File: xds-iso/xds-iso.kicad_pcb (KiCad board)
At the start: 2 copper layers, 82 x 33 mm, 109 parts, among them J1 USB4085, J2 TGT_JTAG, J3 IF_JTAG, J4 Conn_01x02_Male, SW2 EVQPUD, U1 MCP1703A-3002_SOT223, U2 MSP432E401Y, U3 ISOW7741, U4 ISOW7741, U5 TPD4E004DRYR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

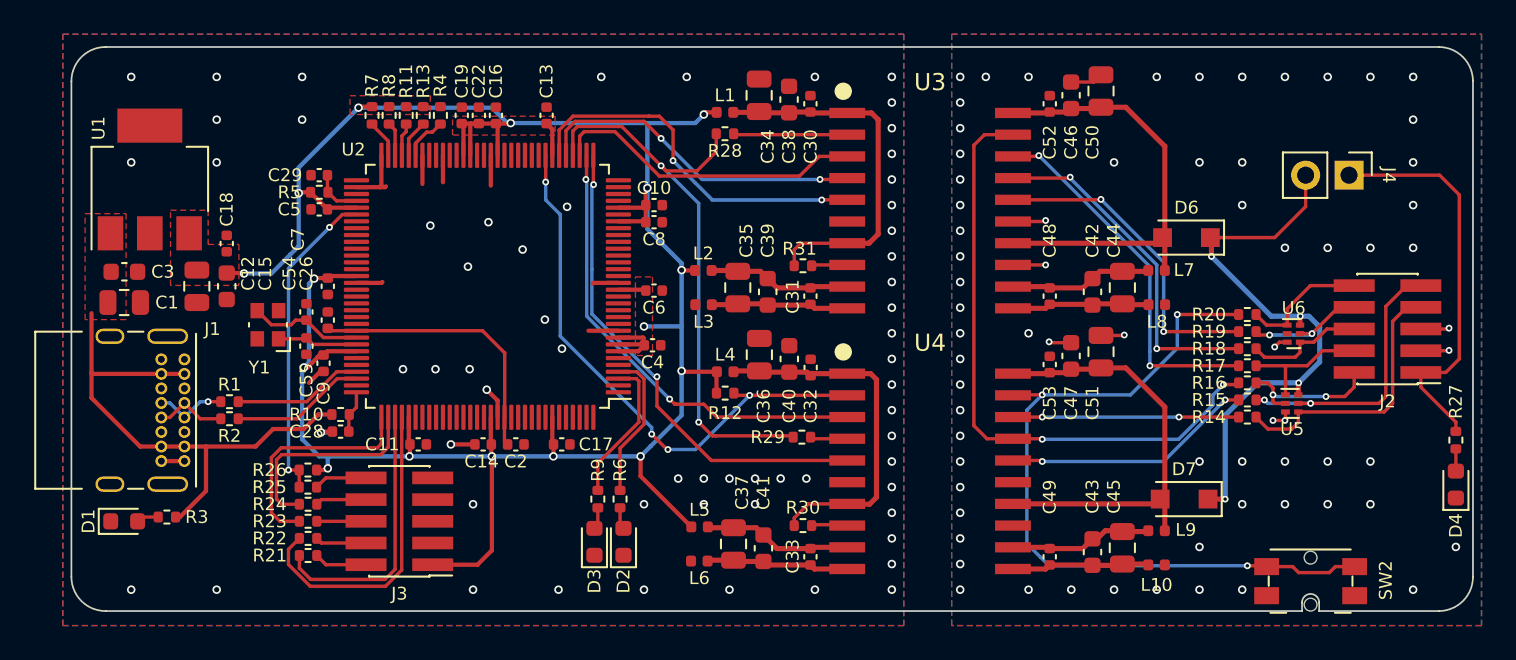
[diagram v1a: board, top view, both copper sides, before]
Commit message: R02 updates supporting cJTAG and SWD
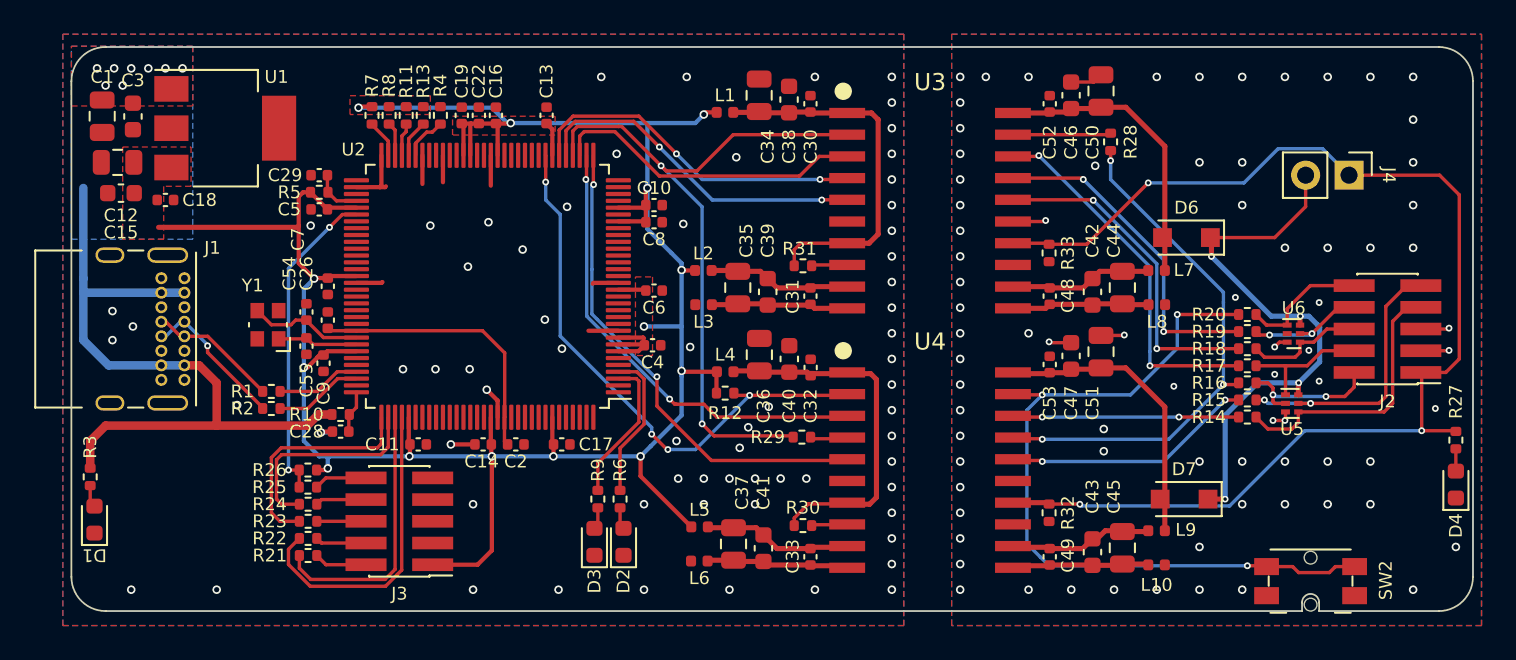
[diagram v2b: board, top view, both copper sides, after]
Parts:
- added R32: 10k, Resistor_SMD:R_0402_1005Metric, F.Cu at (158.7, 103.0)
- added R33: 10k, Resistor_SMD:R_0402_1005Metric, F.Cu at (158.7, 87.8)
- R28: value 100R -> 1K
- R29: value 100R-DNP -> 100R
- U4: value ISOW7741 -> ISOW7742
- moved R28 22.6 mm to (162.3, 81.3), turned to -90 degrees
- moved C1 11.0 mm to (103.3, 79.8), turned to 90 degrees
- moved C3 9.10 mm to (105.1, 79.8), turned to 90 degrees
- moved C12 8.61 mm to (104.2, 82.5), turned to 0 degrees
- moved C15 8.25 mm to (104.4, 84.3), turned to 0 degrees
- moved U1 5.34 mm to (110.5, 80.5), turned to 0 degrees
- moved R3 5.07 mm to (102.6, 100.9), turned to 90 degrees
- moved J1 4.75 mm to (108.1, 89.3)
- moved C18 4.40 mm to (107.0, 84.7), turned to 180 degrees
- moved R1 2.52 mm to (113.2, 95.9)
- moved R2 2.52 mm to (113.2, 96.9)
- moved D1 1.74 mm to (102.8, 103.4), turned to 90 degrees
- moved U4 0.07 mm to (151.7, 100.5)
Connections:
- R28 pad 1: /XDS_TMS -> Net-(R28-Pad1)
- R28 pad 2: Net-(R28-Pad2) -> /ISO_TMS
- U3 pad 14: Net-(C46-Pad1) -> /V_{TGT}
- U3 pad 16: /ISO_TDI -> /ISO_TDO
- U3 pad 17: /ISO_TDO -> /ISO_TDI
- U3 pad 19: /ISO_TMS -> Net-(R28-Pad1)
- U3 pad 2: Net-(R28-Pad2) -> /XDS_TMS
- U3 pad 4: /XDS_TDO -> /XDS_TDI
- U3 pad 5: /XDS_TDI -> /XDS_TDO
- U4 pad 14: Net-(C47-Pad1) -> /V_{TGT}
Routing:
- net /V_{TGT}: track 23.4 -> 72.9 mm, vias 0 -> 3
- net +5V: track 31.4 -> 42.5 mm, vias 0 -> 8
- net Net-(C46-Pad1): track 26.2 -> 17.3 mm
- net Net-(C47-Pad1): track 26.1 -> 17.3 mm
- net /XDS_TMS: track 34.3 -> 41.3 mm
- net Net-(R28-Pad2): track 6.66 -> 0.00 mm
- net Net-(R28-Pad1): track 0.00 -> 5.75 mm
- net /ISO_TMS: track 36.5 -> 31.0 mm, vias 2 -> 3
- net Net-(J1-PadA6): track 4.21 -> 8.67 mm, vias 0 -> 1
- net Net-(J1-PadA7): track 4.21 -> 7.62 mm, vias 1 -> 0
- net /USB_DM: track 7.64 -> 4.94 mm
- net /USB_DP: track 7.89 -> 5.19 mm
- net GND: track 20.7 -> 18.2 mm, vias 61 -> 67
- net GND1: track 13.8 -> 11.9 mm, vias 69 -> 77
- net /XDS_TDI: track 21.8 -> 20.2 mm
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- added copper zone on B.Cu, net +5V
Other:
- board text added: "r0.2"
- board text removed: "r0.1"

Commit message: Changed TMS series resistor to 1k
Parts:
- R29: value 100R -> 1k
- U1: value MCP1703A-3002_SOT223 -> AP7361EA-33E-13
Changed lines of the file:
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@@
       (effects (font (size 0.75 0.75) (thickness 0.15)))
     )
-    (fp_text value "MCP1703A-3002_SOT223" (at 0 4.5) (layer "F.Fab")
+    (fp_text value "AP7361EA-33E-13" (at 0 4.5) (layer "F.Fab")
       (effects (font (size 1 1) (thickness 0.15)))
     )
@@
       (effects (font (size 0.75 0.75) (thickness 0.15)))
     )
-    (fp_text value "100R" (at 0 1.17) (layer "F.Fab")
-      (effects (font (size 1 1) (thickness 0.15)))
-    )
+    (fp_text value "1k" (at 0 1.17) (layer "F.Fab")
+      (effects (font (size 1 1) (thickness 0.15)))
+    )

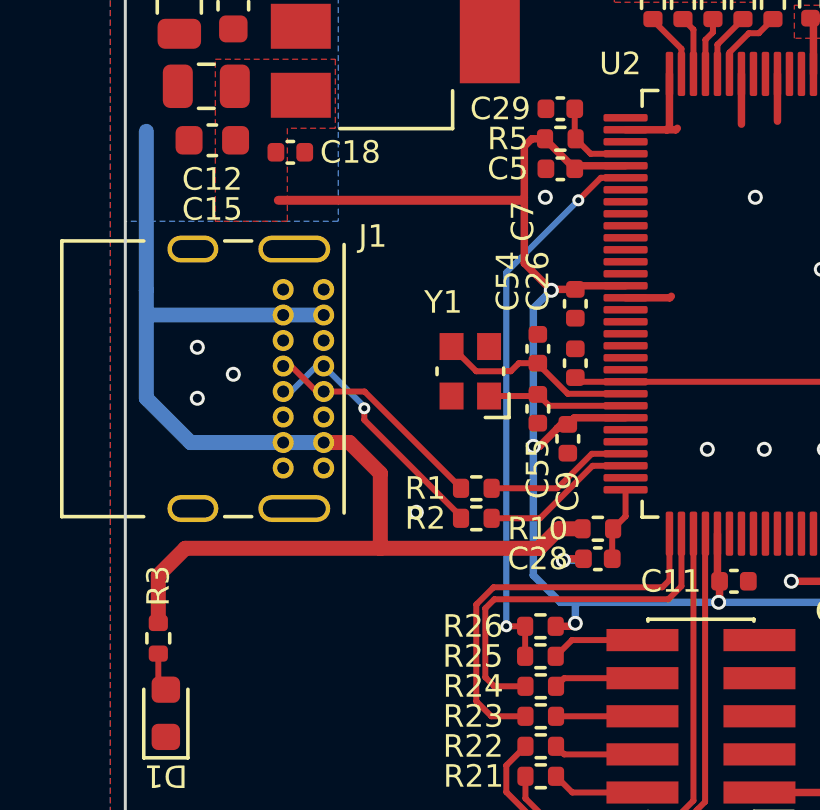
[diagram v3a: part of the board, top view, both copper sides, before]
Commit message: Added 5.1k pulldowns to the CC1 and CC2 pins to comply with USB Type C spec
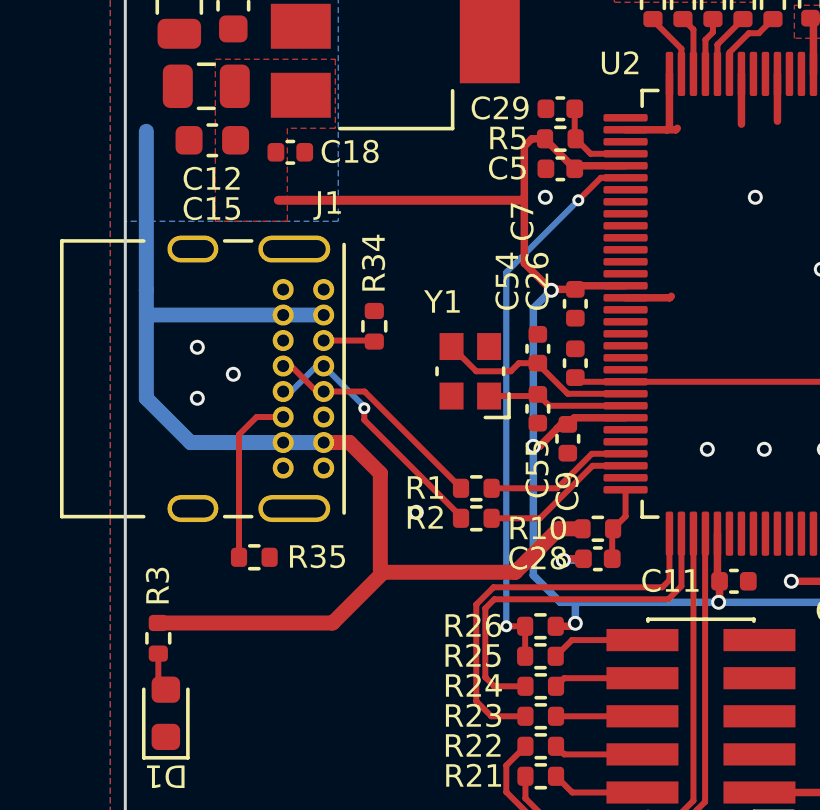
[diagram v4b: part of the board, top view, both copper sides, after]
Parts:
- added R34: 5.1k, Resistor_SMD:R_0402_1005Metric, F.Cu at (109.8, 90.5)
- added R35: 5.1k, Resistor_SMD:R_0402_1005Metric, F.Cu at (105.8, 98.2)
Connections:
- J1 pad A5: unconnected-(J1-PadA5) -> /CC1
- J1 pad B5: unconnected-(J1-PadB5) -> /CC2
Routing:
- net /CC2: track 0.00 -> 5.80 mm
- net /CC1: track 0.00 -> 1.70 mm
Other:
- board text added: "r0.2b"
- board text removed: "r0.2"
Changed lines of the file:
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@@
     )
     (pad_to_mask_clearance 0)
+    (grid_origin 110 87.5)
     (pcbplotparams
       (layerselection 0x00010fc_ffffffff)
@@
   (net 23 "Net-(D4-Pad2)")
   (net 24 "/V_{ISOOUT}")
-  (net 25 "unconnected-(J1-PadA5)")
+  (net 25 "/CC1")
   (net 26 "Net-(J1-PadA6)")
   (net 27 "Net-(J1-PadA7)")
   (net 28 "unconnected-(J1-PadA8)")
-  (net 29 "unconnected-(J1-PadB5)")
+  (net 29 "/CC2")
   (net 30 "unconnected-(J1-PadB8)")
   (net 31 "/V_{TGT}")
@@
     (property "Sheetname" "")
     (attr through_hole)
-    (fp_text reference "J1" (at -1.775 -1.6375 unlocked) (layer "F.SilkS")
+    (fp_text reference "J1" (at -2.875 -0.1875 unlocked) (layer "F.SilkS")
       (effects (font (size 0.75 0.75) (thickness 0.15)))
     )
@@
       (net 2 "+5V") (pinfunction "VBUS") (pintype "passive"))
     (pad "A5" thru_hole circle (at 1.7 0 270) (size 0.7 0.7) (drill 0.4) (layers *.Cu *.Mask)
-      (net 25 "unconnected-(J1-PadA5)") (pinfunction "CC1") (pintype "bidirectional+no_connect"))
+      (net 25 "/CC1") (pinfunction "CC1") (pintype "bidirectional"))
     (pad "A6" thru_hole circle (at 2.55 0 270) (size 0.7 0.7) (drill 0.4) (layers *.Cu *.Mask)
       (net 26 "Net-(J1-PadA6)") (pinfunction "D+") (pintype "bidirectional"))
@@
       (net 2 "+5V") (pinfunction "VBUS") (pintype "passive"))
     (pad "B5" thru_hole circle (at 4.25 1.35 270) (size 0.7 0.7) (drill 0.4) (layers *.Cu *.Mask)
-      (net 29 "unconnected-(J1-PadB5)") (pinfunction "CC2") (pintype "bidirectional+no_connect"))
+      (net 29 "/CC2") (pinfunction "CC2") (pintype "bidirectional"))
     (pad "B6" thru_hole circle (at 3.4 1.35 270) (size 0.7 0.7) (drill 0.4) (layers *.Cu *.Mask)
       (net 26 "Net-(J1-PadA6)") (pinfunction "D+") (pintype "bidirectional"))
@@
   )
   (footprint "Resistor_SMD:R_0402_1005Metric" (layer "F.Cu")
+    (at 109.8 90.5 -90)
+    (descr "Resistor SMD 0402 (1005 Metric), square (rectangular) end terminal, IPC_7351 nominal, (Body size source: IPC-SM-782 page 72, https://www.pcb-3d.com/wordpress/wp-content/uploads/ipc-sm-782a_amendment_1_and_2.pdf), generated with kicad-footprint-generator")
+    (tags "resistor")
+    (property "Sheetfile" "xds-iso.kicad_sch")
+    (property "Sheetname" "")
+    (attr smd)
+    (fp_text reference "R34" (at -2.1 0 90) (layer "F.SilkS")
+      (effects (font (size 0.75 0.75) (thickness 0.15)))
+    )
+    (fp_text value "5.1k" (at 0 1.17 90) (layer "F.Fab")
+      (effects (font (size 1 1) (thickness 0.15)))
+    )
+    (fp_text user "${REFERENCE}" (at 0 0 90) (layer "F.Fab")
+      (effects (font (size 0.26 0.26) (thickness 0.04)))
+    )
+    (fp_line (start -0.153641 0.38) (end 0.153641 0.38) (layer "F.SilkS") (width 0.12))
+    (fp_line (start -0.153641 -0.38) (end 0.153641 -0.38) (layer "F.SilkS") (width 0.12))
+    (fp_line (start -0.93 -0.47) (end 0.93 -0.47) (layer "F.CrtYd") (width 0.05))
+    (fp_line (start -0.93 0.47) (end -0.93 -0.47) (layer "F.CrtYd") (width 0.05))
+    (fp_line (start 0.93 -0.47) (end 0.93 0.47) (layer "F.CrtYd") (width 0.05))
+    (fp_line (start 0.93 0.47) (end -0.93 0.47) (layer "F.CrtYd") (width 0.05))
+    (fp_line (start -0.525 0.27) (end -0.525 -0.27) (layer "F.Fab") (width 0.1))
+    (fp_line (start 0.525 -0.27) (end 0.525 0.27) (layer "F.Fab") (width 0.1))
+    (fp_line (start 0.525 0.27) (end -0.525 0.27) (layer "F.Fab") (width 0.1))
+    (fp_line (start -0.525 -0.27) (end 0.525 -0.27) (layer "F.Fab") (width 0.1))
+    (pad "1" smd roundrect (at -0.51 0 270) (size 0.54 0.64) (layers "F.Cu" "F.Paste" "F.Mask") (roundrect_rratio 0.25)
+      (net 1 "GND") (pintype "passive"))
+    (pad "2" smd roundrect (at 0.51 0 270) (size 0.54 0.64) (layers "F.Cu" "F.Paste" "F.Mask") (roundrect_rratio 0.25)
+      (net 25 "/CC1") (pintype "passive"))
+    (model "${KICAD6_3DMODEL_DIR}/Resistor_SMD.3dshapes/R_0402_1005Metric.wrl"
+      (offset (xyz 0 0 0))
+      (scale (xyz 1 1 1))
+      (rotate (xyz 0 0 0))
+    )
+  )
+  (footprint "Resistor_SMD:R_0402_1005Metric" (layer "F.Cu")
     (at 170.3 97.4)
     (descr "Resistor SMD 0402 (1005 Metric), square (rectangular) end terminal, IPC_7351 nominal, (Body size source: IPC-SM-782 page 72, https://www.pcb-3d.com/wordpress/wp-content/uploads/ipc-sm-782a_amendment_1_and_2.pdf), generated with kicad-footprint-generator")
@@
   )
   (footprint "Resistor_SMD:R_0402_1005Metric" (layer "F.Cu")
+    (at 105.8 98.2 180)
+    (descr "Resistor SMD 0402 (1005 Metric), square (rectangular) end terminal, IPC_7351 nominal, (Body size source: IPC-SM-782 page 72, https://www.pcb-3d.com/wordpress/wp-content/uploads/ipc-sm-782a_amendment_1_and_2.pdf), generated with kicad-footprint-generator")
+    (tags "resistor")
+    (property "Sheetfile" "xds-iso.kicad_sch")
+    (property "Sheetname" "")
+    (attr smd)
+    (fp_text reference "R35" (at -2.1 0) (layer "F.SilkS")
+      (effects (font (size 0.75 0.75) (thickness 0.15)))
+    )
+    (fp_text value "5.1k" (at 0 1.17) (layer "F.Fab")
+      (effects (font (size 1 1) (thickness 0.15)))
+    )
+    (fp_text user "${REFERENCE}" (at 0 0) (layer "F.Fab")
+      (effects (font (size 0.26 0.26) (thickness 0.04)))
+    )
+    (fp_line (start -0.153641 -0.38) (end 0.153641 -0.38) (layer "F.SilkS") (width 0.12))
+    (fp_line (start -0.153641 0.38) (end 0.153641 0.38) (layer "F.SilkS") (width 0.12))
+    (fp_line (start -0.93 0.47) (end -0.93 -0.47) (layer "F.CrtYd") (width 0.05))
+    (fp_line (start 0.93 0.47) (end -0.93 0.47) (layer "F.CrtYd") (width 0.05))
+    (fp_line (start -0.93 -0.47) (end 0.93 -0.47) (layer "F.CrtYd") (width 0.05))
+    (fp_line (start 0.93 -0.47) (end 0.93 0.47) (layer "F.CrtYd") (width 0.05))
+    (fp_line (start 0.525 0.27) (end -0.525 0.27) (layer "F.Fab") (width 0.1))
+    (fp_line (start 0.525 -0.27) (end 0.525 0.27) (layer "F.Fab") (width 0.1))
+    (fp_line (start -0.525 0.27) (end -0.525 -0.27) (layer "F.Fab") (width 0.1))
+    (fp_line (start -0.525 -0.27) (end 0.525 -0.27) (layer "F.Fab") (width 0.1))
+    (pad "1" smd roundrect (at -0.51 0 180) (size 0.54 0.64) (layers "F.Cu" "F.Paste" "F.Mask") (roundrect_rratio 0.25)
+      (net 1 "GND") (pintype "passive"))
+    (pad "2" smd roundrect (at 0.51 0 180) (size 0.54 0.64) (layers "F.Cu" "F.Paste" "F.Mask") (roundrect_rratio 0.25)
+      (net 29 "/CC2") (pintype "passive"))
+    (model "${KICAD6_3DMODEL_DIR}/Resistor_SMD.3dshapes/R_0402_1005Metric.wrl"
+      (offset (xyz 0 0 0))
+      (scale (xyz 1 1 1))
+      (rotate (xyz 0 0 0))
+    )
+  )
+  (footprint "Resistor_SMD:R_0402_1005Metric" (layer "F.Cu")
     (at 170.3 91.4 180)
     (descr "Resistor SMD 0402 (1005 Metric), square (rectangular) end terminal, IPC_7351 nominal, (Body size source: IPC-SM-782 page 72, https://www.pcb-3d.com/wordpress/wp-content/uploads/ipc-sm-782a_amendment_1_and_2.pdf), generated with kicad-footprint-generator")
@@
     (effects (font (size 1 1) (thickness 0.15)) (justify mirror))
   )
-  (gr_text "r0.2" (at 154.6 92.25 90) (layer "B.Mask")
+  (gr_text "r0.2b" (at 154.6 92.25 90) (layer "B.Mask")
     (effects (font (size 1 1) (thickness 0.25)) (justify mirror))
   )
@@
   (segment (start 116.1 98.3) (end 116.7 98.3) (width 0.25) (layer "B.Cu") (net 1))
   (segment (start 116.7 98.3) (end 116.8 98.2) (width 0.25) (layer "B.Cu") (net 1))
-  (segment (start 103.5 97.9) (end 102.6 98.8) (width 0.5) (layer "F.Cu") (net 2))
-  (segment (start 110 97.9) (end 103.5 97.9) (width 0.5) (layer "F.Cu") (net 2))
-  (segment (start 110 95.4) (end 110 97.9) (width 0.5) (layer "F.Cu") (net 2))
-  (segment (start 110 97.9) (end 115.3 97.9) (width 0.5) (layer "F.Cu") (net 2))
-  (segment (start 115.3 97.9) (end 115.95 97.25) (width 0.5) (layer "F.Cu") (net 2))
+  (segment (start 110 98.6) (end 110.1 98.7) (width 0.5) (layer "F.Cu") (net 2))
+  (segment (start 116.74 97.25) (end 115.95 97.25) (width 0.5) (layer "F.Cu") (net 2))
+  (segment (start 110.1 98.7) (end 108.41 100.39) (width 0.5) (layer "F.Cu") (net 2))
   (segment (start 108.975 94.375) (end 110 95.4) (width 0.5) (layer "F.Cu") (net 2))
-  (segment (start 102.6 98.8) (end 102.6 100.39) (width 0.5) (layer "F.Cu") (net 2))
-  (segment (start 115.95 97.25) (end 116.74 97.25) (width 0.5) (layer "F.Cu") (net 2))
+  (segment (start 110 95.4) (end 110 98.6) (width 0.5) (layer "F.Cu") (net 2))
+  (segment (start 115.95 97.25) (end 114.5 98.7) (width 0.5) (layer "F.Cu") (net 2))
+  (segment (start 114.5 98.7) (end 110.1 98.7) (width 0.5) (layer "F.Cu") (net 2))
+  (segment (start 108.41 100.39) (end 102.6 100.39) (width 0.5) (layer "F.Cu") (net 2))
   (segment (start 108.1125 94.375) (end 108.975 94.375) (width 0.5) (layer "F.Cu") (net 2))
   (via (at 103.5 78) (size 0.5) (drill 0.3) (layers "F.Cu" "B.Cu") (net 2))
@@
   (segment (start 173.4 91.5) (end 171.7 91.5) (width 0.3) (layer "B.Cu") (net 24))
   (segment (start 173.3 95.4) (end 174.531111 94.168889) (width 0.3) (layer "B.Cu") (net 24))
+  (segment (start 109.765 90.975) (end 109.8 91.01) (width 0.2) (layer "F.Cu") (net 25))
+  (segment (start 108.1125 90.975) (end 109.765 90.975) (width 0.2) (layer "F.Cu") (net 25))
   (segment (start 112.69 96.845) (end 112.69 96.9) (width 0.2) (layer "F.Cu") (net 26))
   (segment (start 109.466379 93.621379) (end 112.69 96.845) (width 0.2) (layer "F.Cu") (net 26))
@@
   (segment (start 106.7625 91.825) (end 107.025 91.825) (width 0.2) (layer "F.Cu") (net 27))
   (segment (start 107.025 91.825) (end 107.875 92.675) (width 0.2) (layer "F.Cu") (net 27))
+  (segment (start 105.29 94.11) (end 105.29 98.2) (width 0.2) (layer "F.Cu") (net 29))
+  (segment (start 105.875 93.525) (end 105.29 94.11) (width 0.2) (layer "F.Cu") (net 29))
+  (segment (start 106.7625 93.525) (end 105.875 93.525) (width 0.2) (layer "F.Cu") (net 29))
   (segment (start 180.5 94.84) (end 180.45 94.79) (width 0.2) (layer "F.Cu") (net 31))
   (segment (start 181.55 83.25) (end 176.25 83.25) (width 0.2) (layer "F.Cu") (net 31))
